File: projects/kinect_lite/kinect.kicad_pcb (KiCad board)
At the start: 2 copper layers, 90 x 26 mm, 22 parts, among them J2 USB_C_Receptacle_USB2.0_16P, J3 Conn_02x05_Odd_Even, U1 LM3670MFX-1.8, U2 AP63203WU

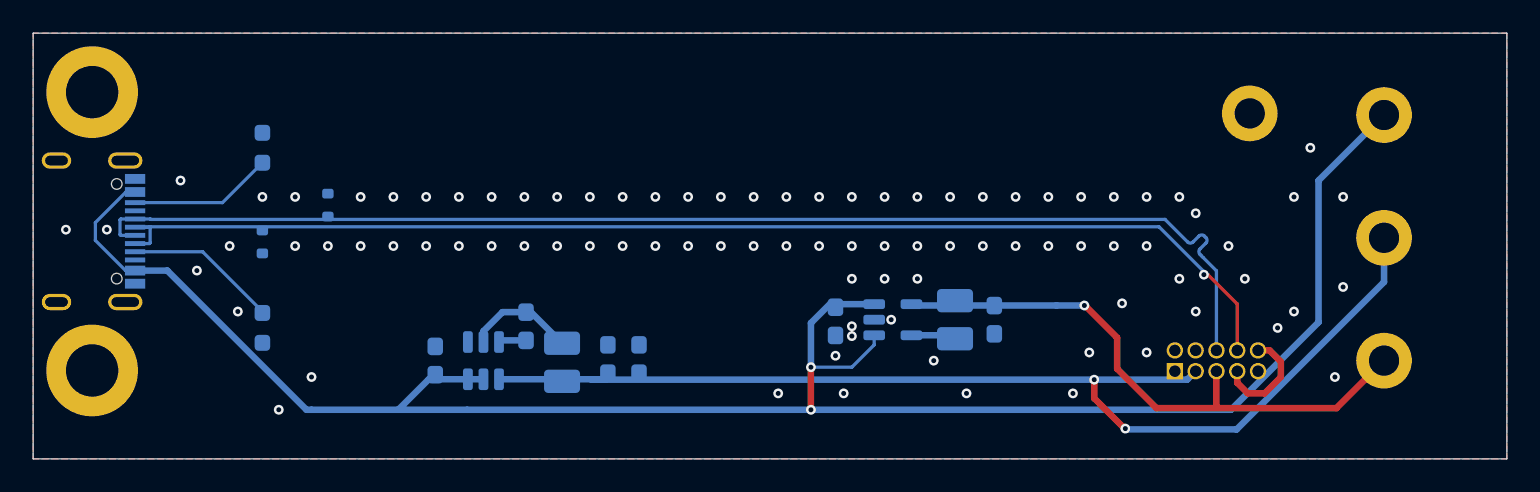
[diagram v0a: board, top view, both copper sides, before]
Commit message: Finish v1 of kinect_lite
Modify silkscreen
Add graphics to copper layer (designed wuth kicad and duckie robot)
round corners of outline
generate Gerbers

Create v2 and v3 of 3D printed cover in FreeCAD
export STL for 3D printing
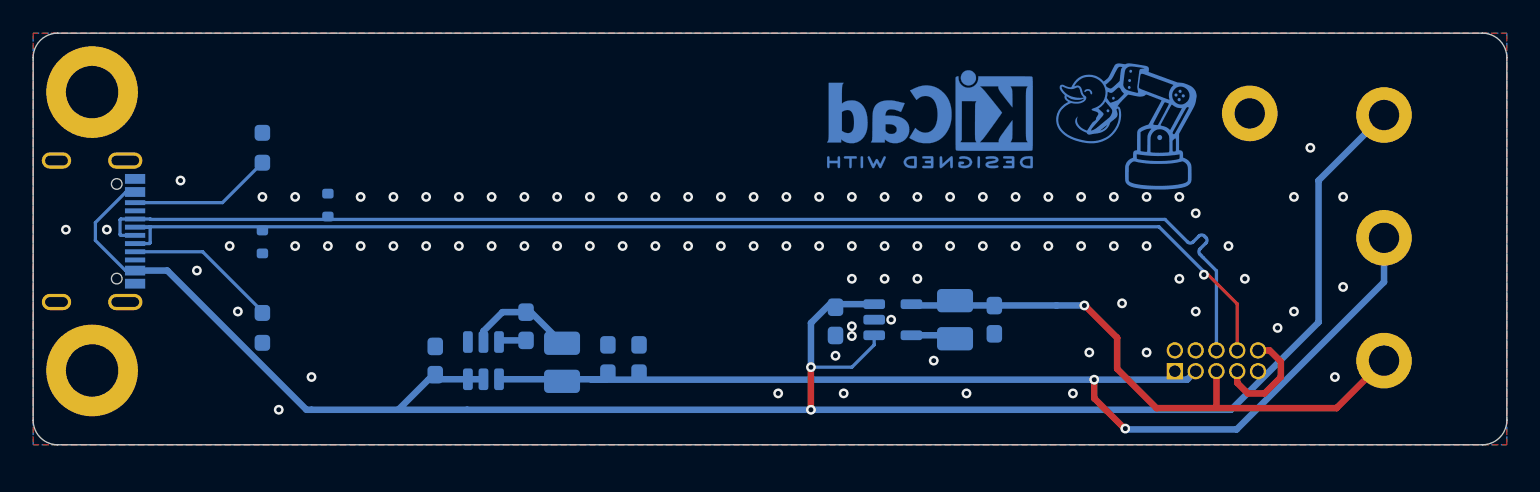
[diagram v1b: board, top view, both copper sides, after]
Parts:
- added G***: LOGO, custom:robot_duckie_logo_10mm, B.Cu at (116.8, 55.2)
- added REF**: KiCad-Logo2_5mm_Copper, Symbol:KiCad-Logo2_5mm_Copper, B.Cu at (104.8, 55.2)
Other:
- board size 90 x 26 mm -> 90 x 25.1 mm
- board text added: "Kinect hacker board v1.0"
- board text added: "USB-C"
- board text removed: "JLCJLCJLCJLC"
- board text removed: "vpl"
